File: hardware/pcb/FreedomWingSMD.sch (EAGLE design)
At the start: 23 parts

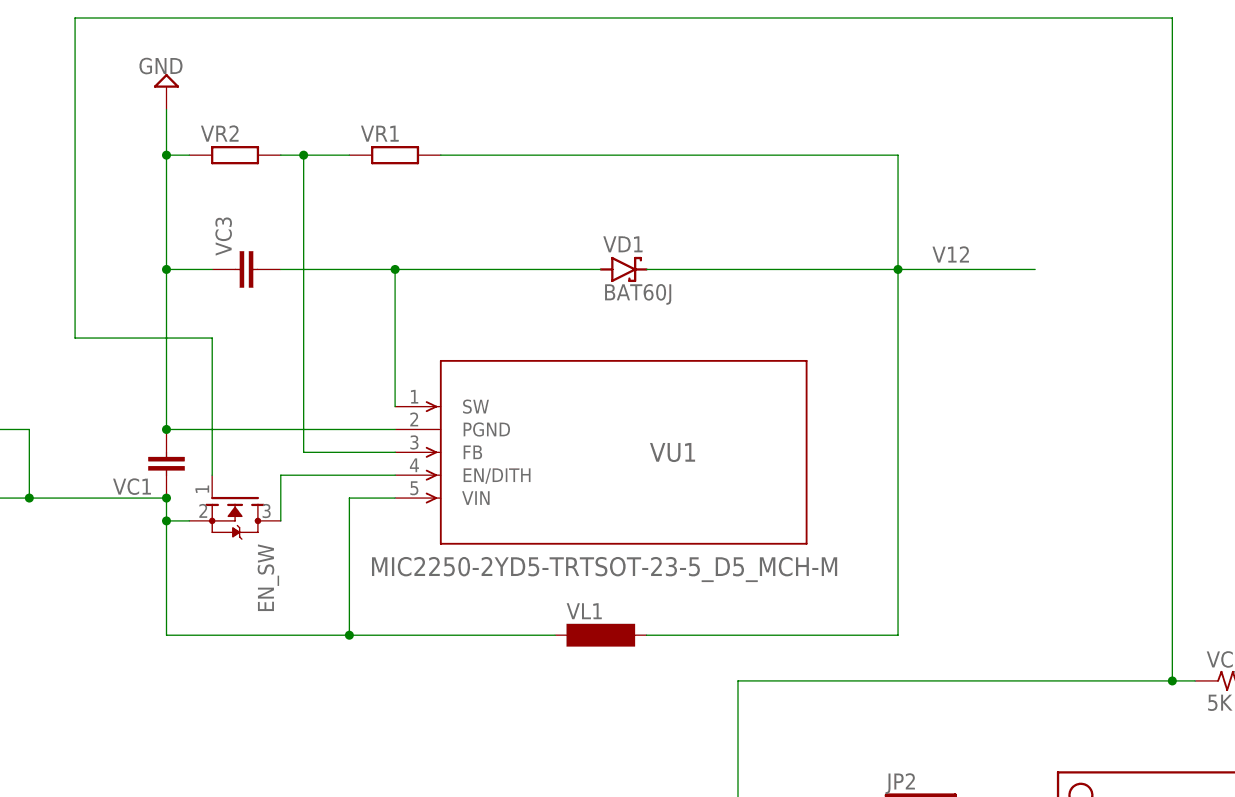
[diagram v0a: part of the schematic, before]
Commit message: Fixed schematic issues w/Voltage Regulator
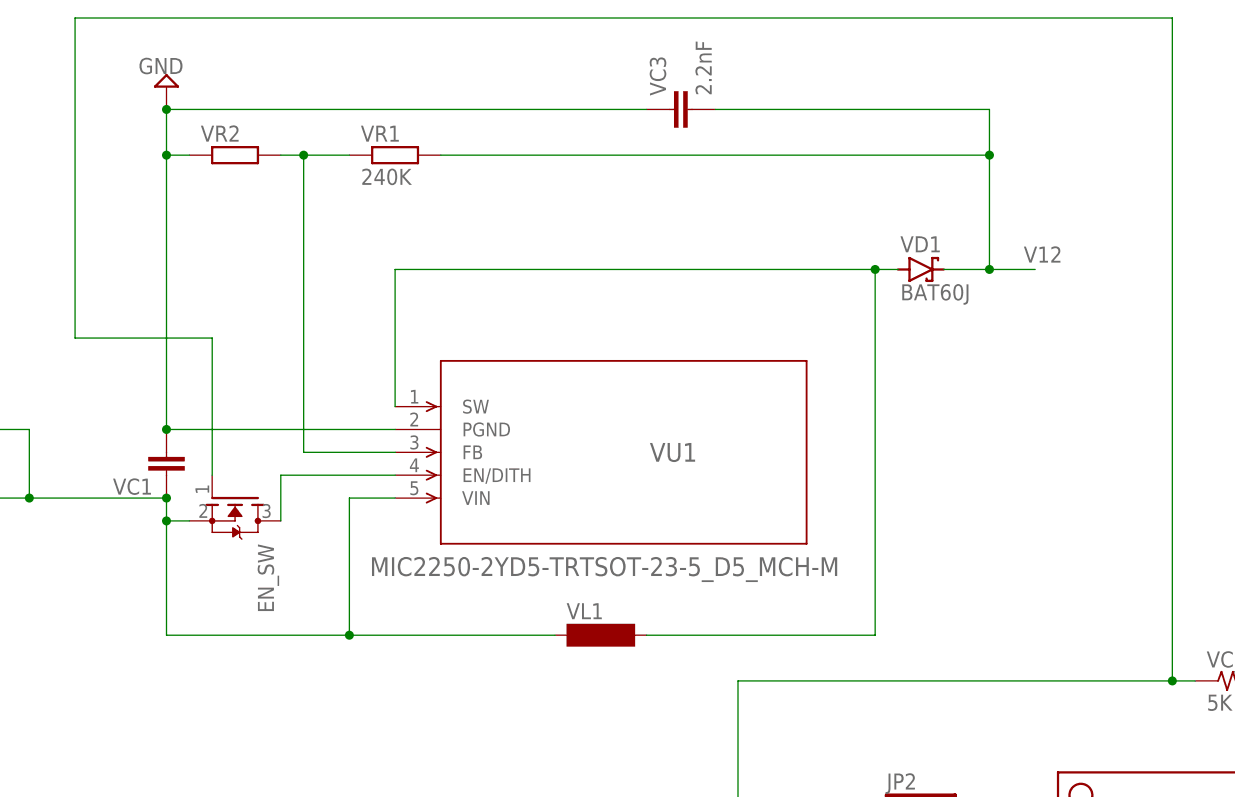
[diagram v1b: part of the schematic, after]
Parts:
- VC3: value (none) -> 2.2nF
- VR1: value (none) -> 240K
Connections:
- net N$26: now also VL1.2; no longer VC3.2
- net V12: now also VC3.2; no longer VL1.2
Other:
- moved on the sheet: VC3, VD1

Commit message: Added values and tweaked for 12V
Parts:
- added VC_ENPIN: (no value), adafruit:PINHD-1X1
- added VR3: 680, rcl:R-EU_R0805W
- VC1: value (none) -> 10mF
- VC3: value 2.2nF -> 2.2mF
- VL1: value (none) -> 10mH
- VR2: value (none) -> 27K
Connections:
- new net N$31: VR2.2, VR3.1
- net N$28: now also VC_ENPIN.1
- net N$8: now also VR3.2; no longer VR2.2
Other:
- moved on the sheet: VR1

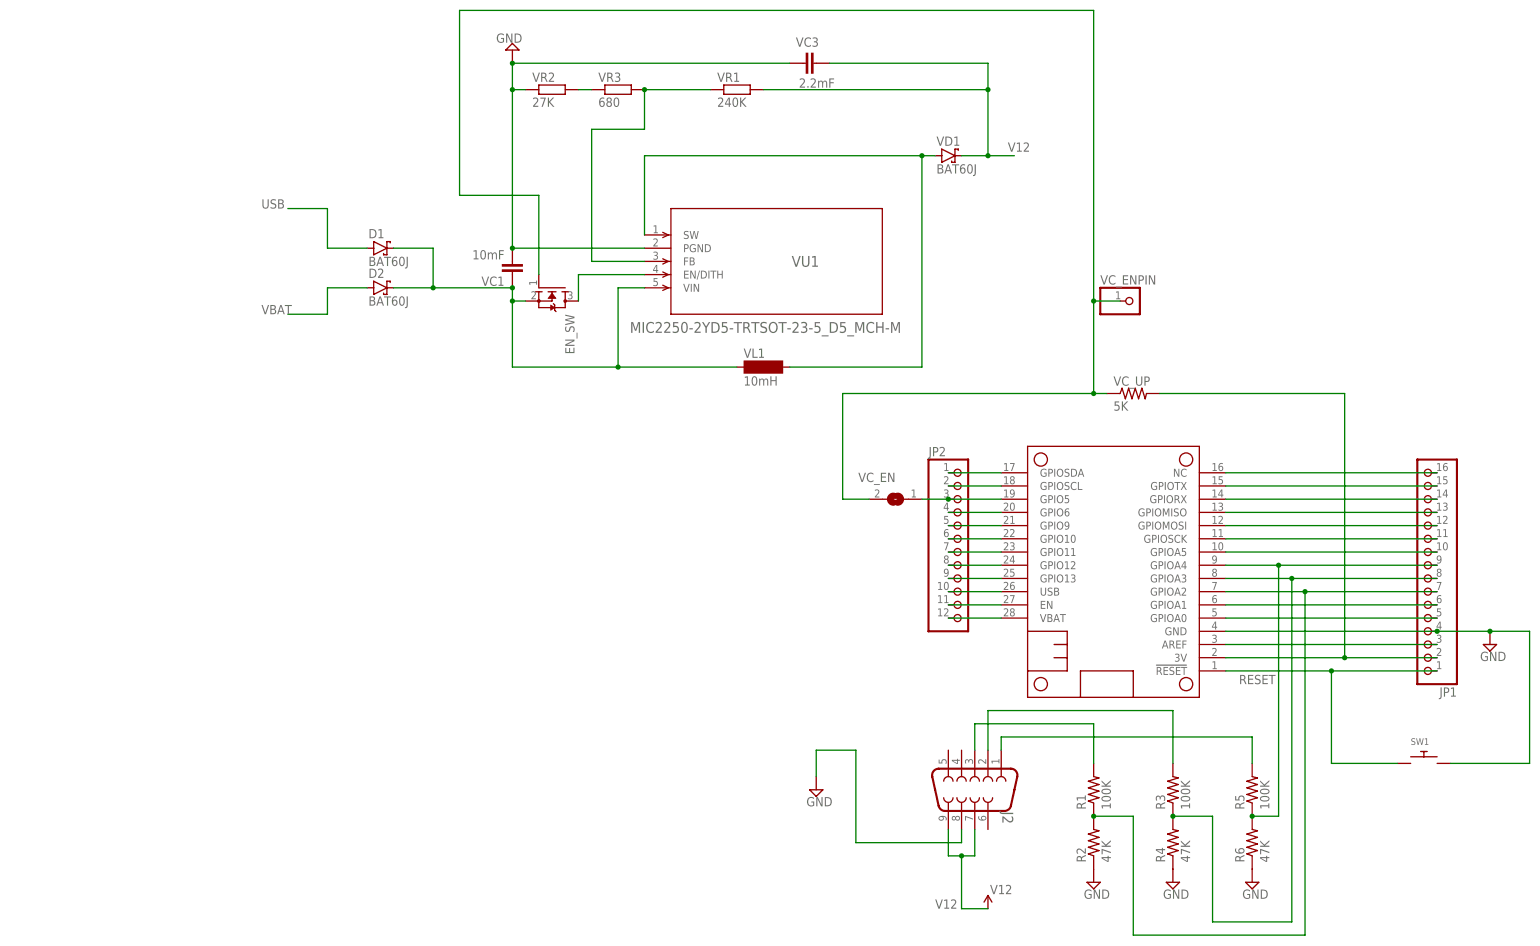
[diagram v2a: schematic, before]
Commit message: Switched to 2 layers & added stuff
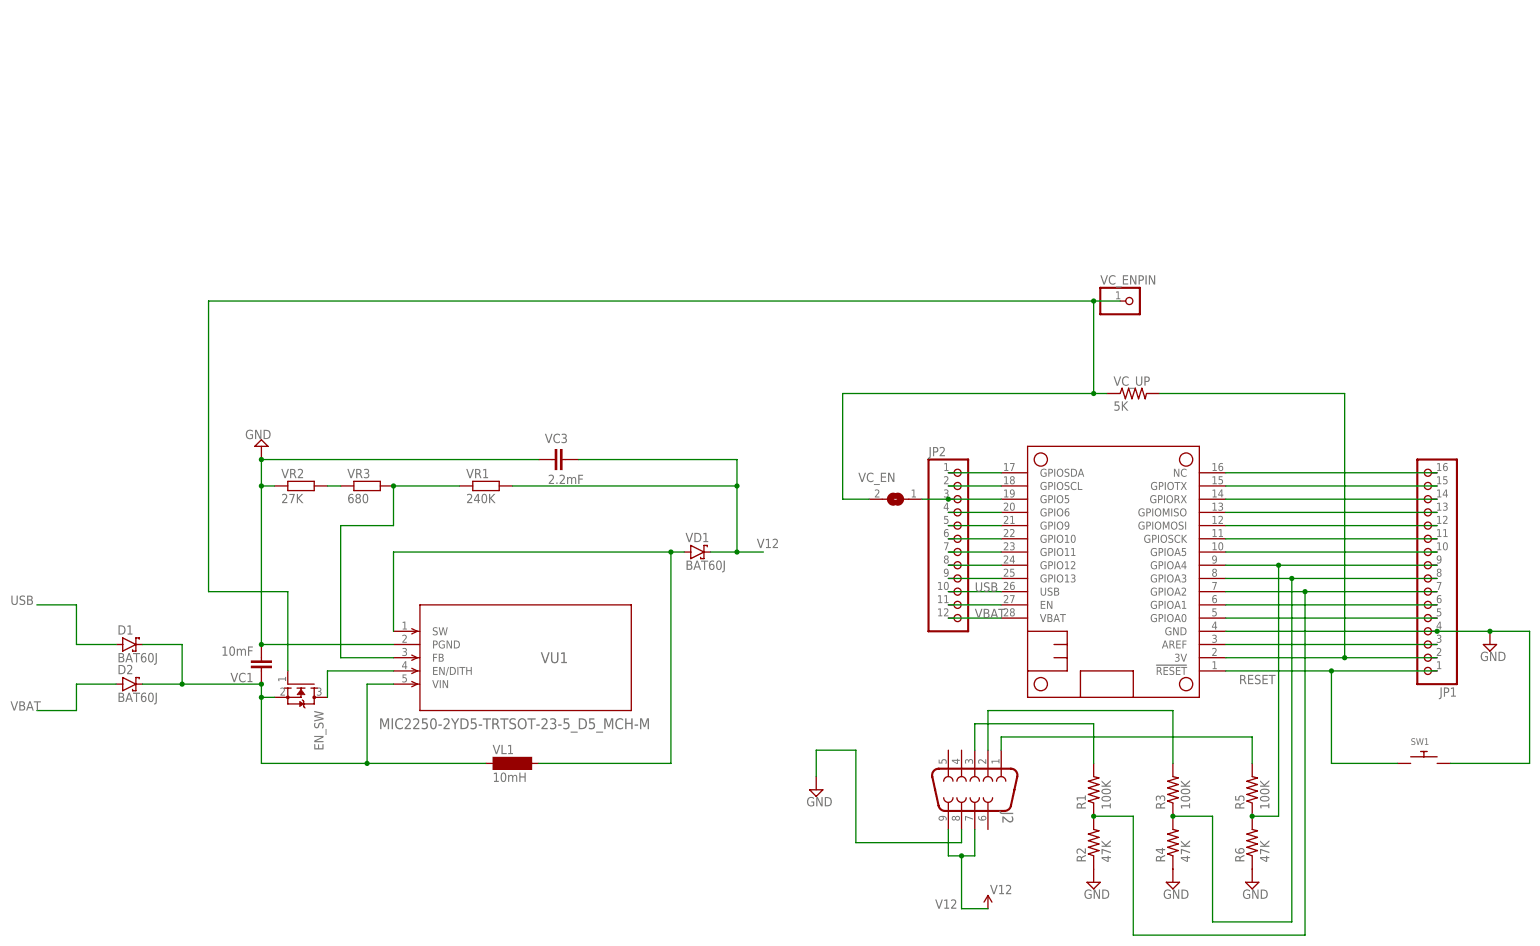
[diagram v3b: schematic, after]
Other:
- moved on the sheet: D1, D2, EN_SW, VC1, VC3, VD1, VL1, VR1, VR2, VR3, VU1
